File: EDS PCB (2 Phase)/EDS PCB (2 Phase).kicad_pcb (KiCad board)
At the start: 2 copper layers, 240 x 127.5 mm, 10 parts

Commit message: Two-Phase and Three-Phase EDS PCBs.
I changed the Two-Phase and Three-Phase EDS PCBs. They just need minor changes now
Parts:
- removed ?: , clipboard:bf32c9e1-eea9-421a-b75f-750c3fb07239
- removed the REF** at (260.5, 144.5)
- removed the REF** at (258.5, 28.0)
- removed the REF** at (29.8, 144.5)
- removed the REF** at (34.2, 110.0)
- removed the REF** at (44.2, 95.0)
- removed the REF** at (70.8, 110.0)
- removed the REF** at (30.0, 26.0)
- removed the REF** at (44.2, 80.0)
- removed the REF** at (44.6, 110.0)
- added REF**: R2, Resistor_THT:R_Axial_DIN0207_L6.3mm_D2.5mm_P15.24mm_Horizontal, F.Cu at (42.8, 80.8)
- added REF**: R1, Resistor_THT:R_Axial_DIN0207_L6.3mm_D2.5mm_P15.24mm_Horizontal, F.Cu at (43.1, 95.8)
- added REF**: MountingHole_3.2mm_M3, MountingHole:MountingHole_3.2mm_M3, F.Cu at (222.5, 157.5)
- added REF**: EDS_Input_Connector, EDS_Project_Library:EDS_Input_Connector, F.Cu at (32.8, 95.8)
- added REF**: MountingHole_3.2mm_M3, MountingHole:MountingHole_3.2mm_M3, F.Cu at (29.5, 157.5)
- added REF**: MountingHole_3.2mm_M3, MountingHole:MountingHole_3.2mm_M3, F.Cu at (29.5, 23.0)
- added REF**: MountingHole_3.2mm_M3, MountingHole:MountingHole_3.2mm_M3, F.Cu at (223.0, 22.5)
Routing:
- net Phase3: track 759.3 -> 0.00 mm
- net Phase1: track 965.2 -> 1417.9 mm
- net Phase2: track 1262.9 -> 1429.9 mm
- net (no net): track 30.4 -> 20.4 mm
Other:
- board size 240 x 127.5 mm -> 203 x 144 mm
- board text removed: "P1"
- board text removed: "P2"
- board text removed: "P3"

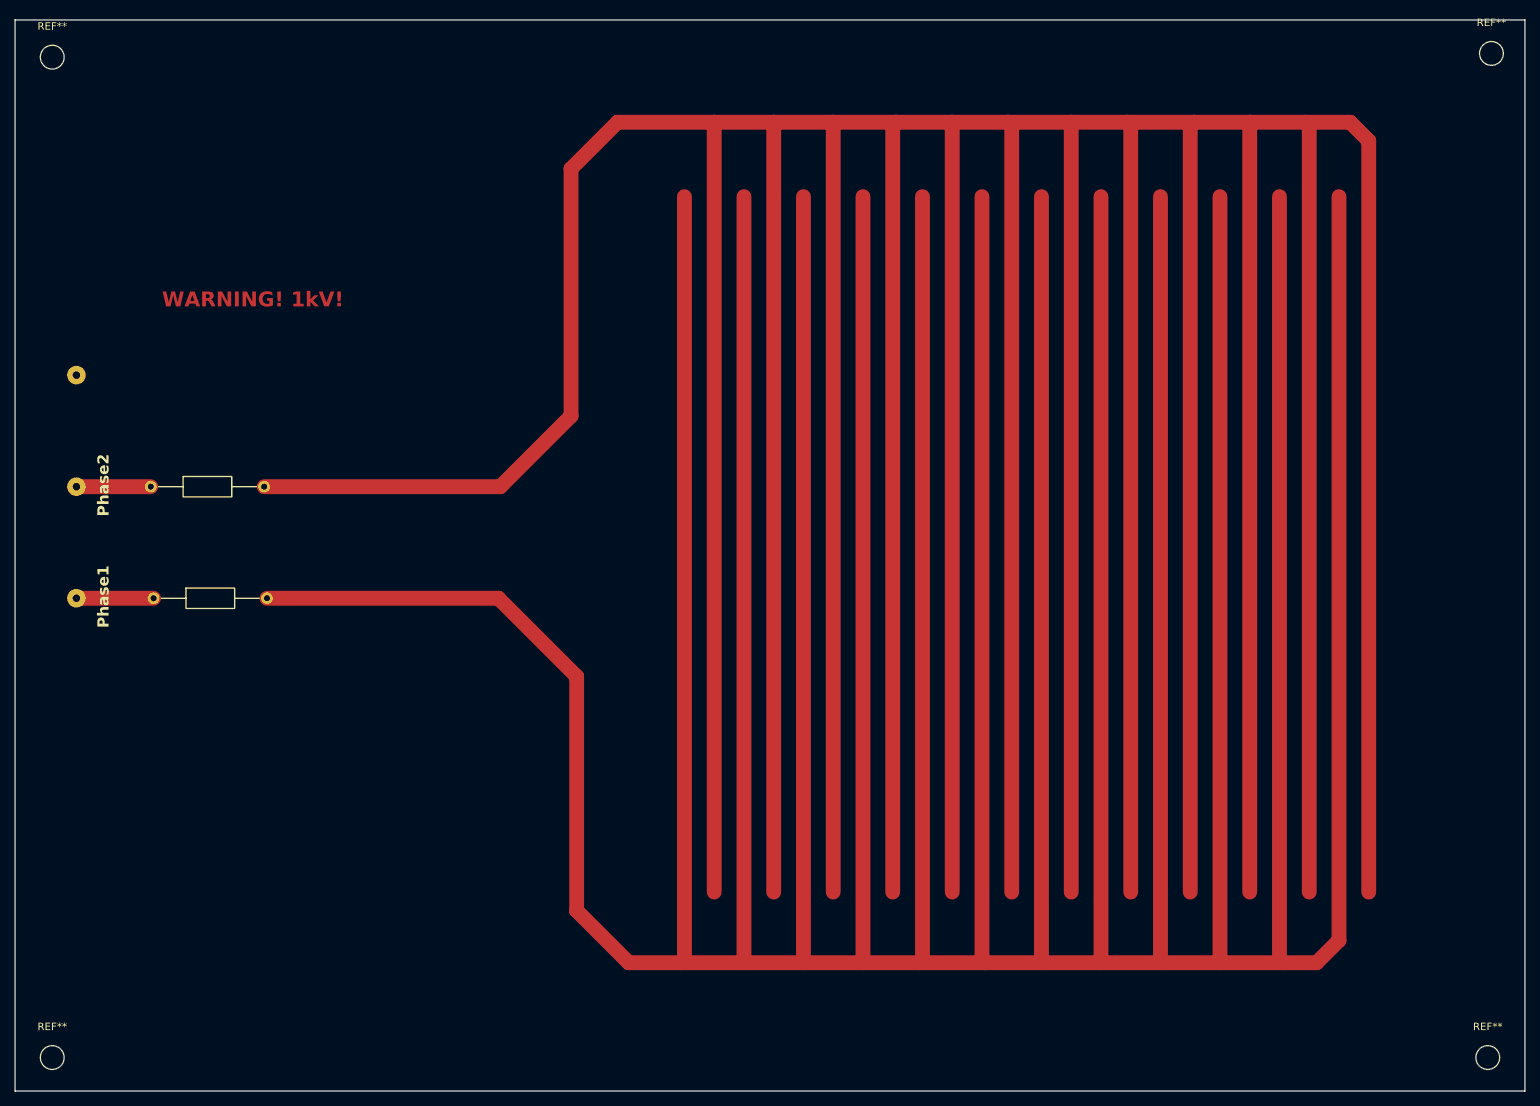
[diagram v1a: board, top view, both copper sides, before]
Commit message: Confirmed Spacing
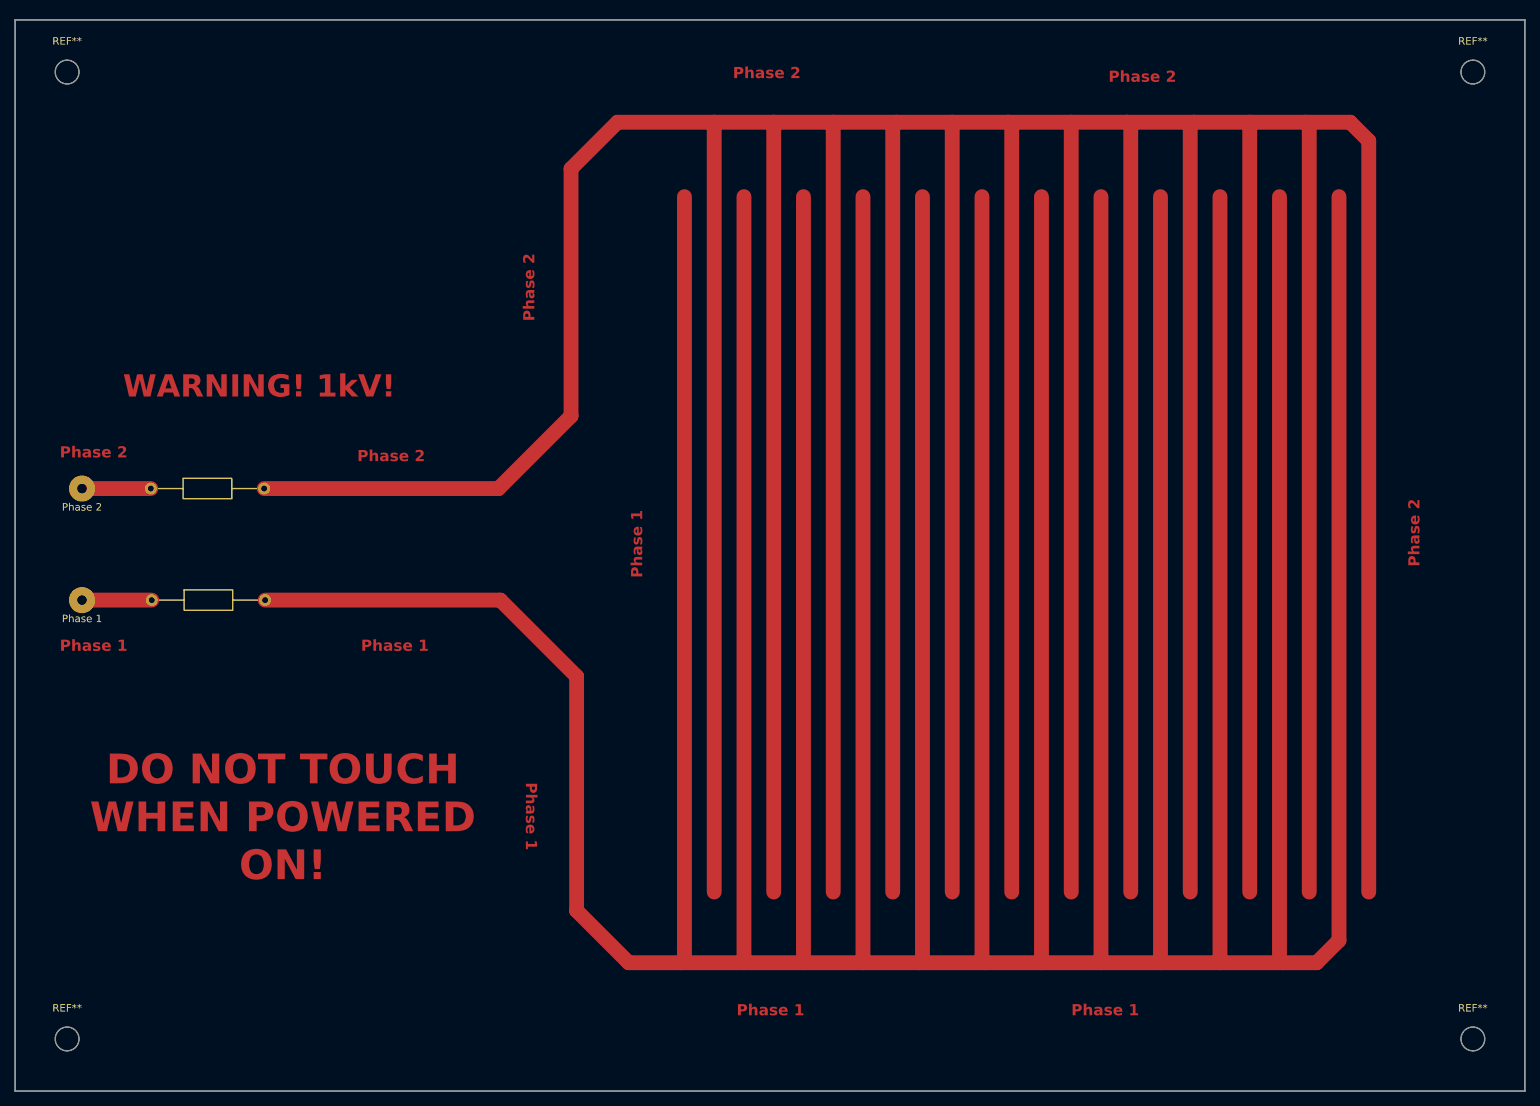
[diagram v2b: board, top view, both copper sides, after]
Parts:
- removed the REF** at (32.8, 95.8)
- added Phase 1: EDS Pad, EDS_Project_Library:EDS Pad, F.Cu at (33.5, 96.0)
- added Phase 2: EDS Pad, EDS_Project_Library:EDS Pad, F.Cu at (33.5, 81.0)
- moved REF** 3.54 mm to (220.5, 25.0)
- moved REF** 3.20 mm to (220.5, 155.0)
- moved REF** 3.20 mm to (31.5, 155.0)
- moved REF** 2.83 mm to (31.5, 25.0)
- moved REF** 0.35 mm to (42.9, 96.0)
- moved REF** 0.25 mm to (42.8, 81.0)
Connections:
- REF** pad 1: (no net) -> Phase2
- REF** pad 1: (no net) -> Phase1
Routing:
- net (no net): track 20.4 -> 0.00 mm
- net Phase1: track 1417.9 -> 1427.5 mm
- net Phase2: track 1429.9 -> 1439.2 mm
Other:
- board text added: "DO NOT TOUCH WHEN POWERED ON!"
- board text added: "Phase 1"
- board text added: "Phase 2"
